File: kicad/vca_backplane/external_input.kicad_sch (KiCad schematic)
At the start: 6 parts, among them J10 AudioJack_729JH, U13 TL072

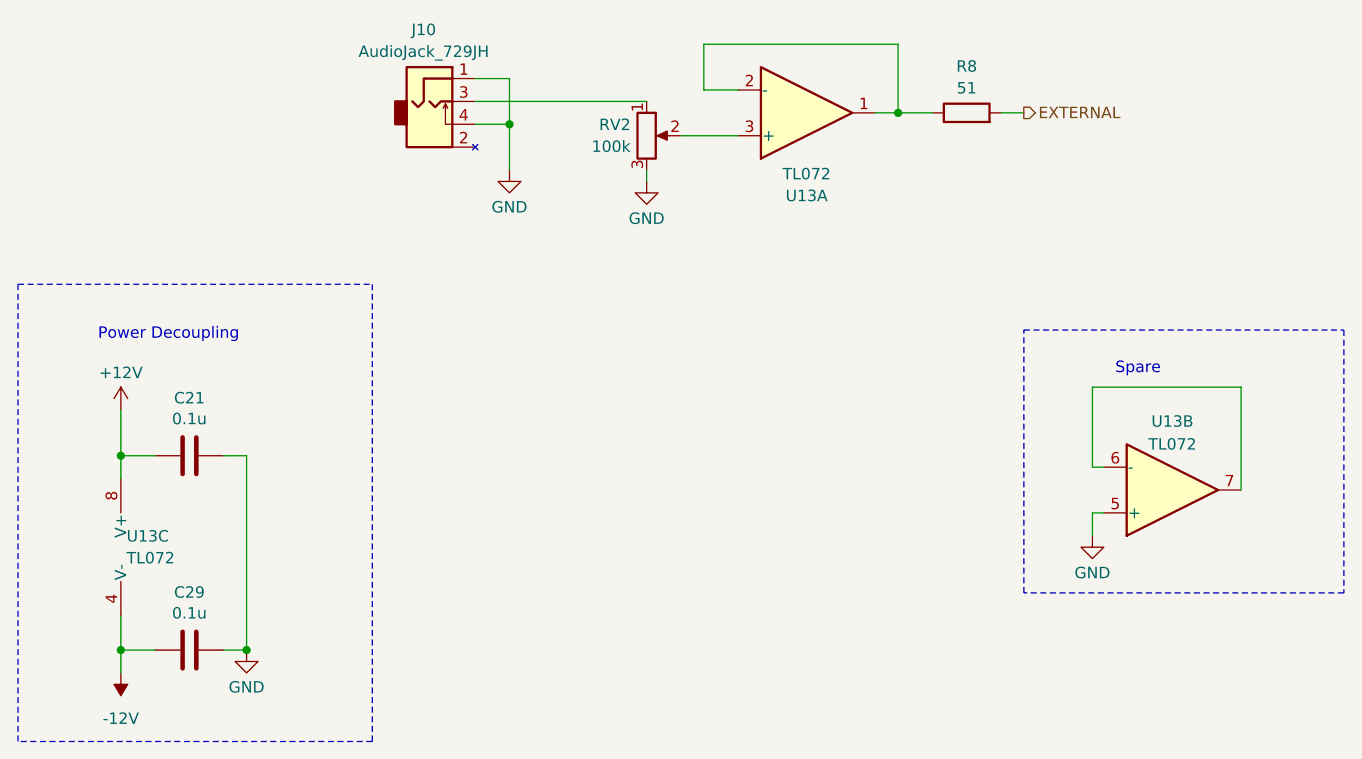
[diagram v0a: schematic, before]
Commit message: geographically reorientated from pcb
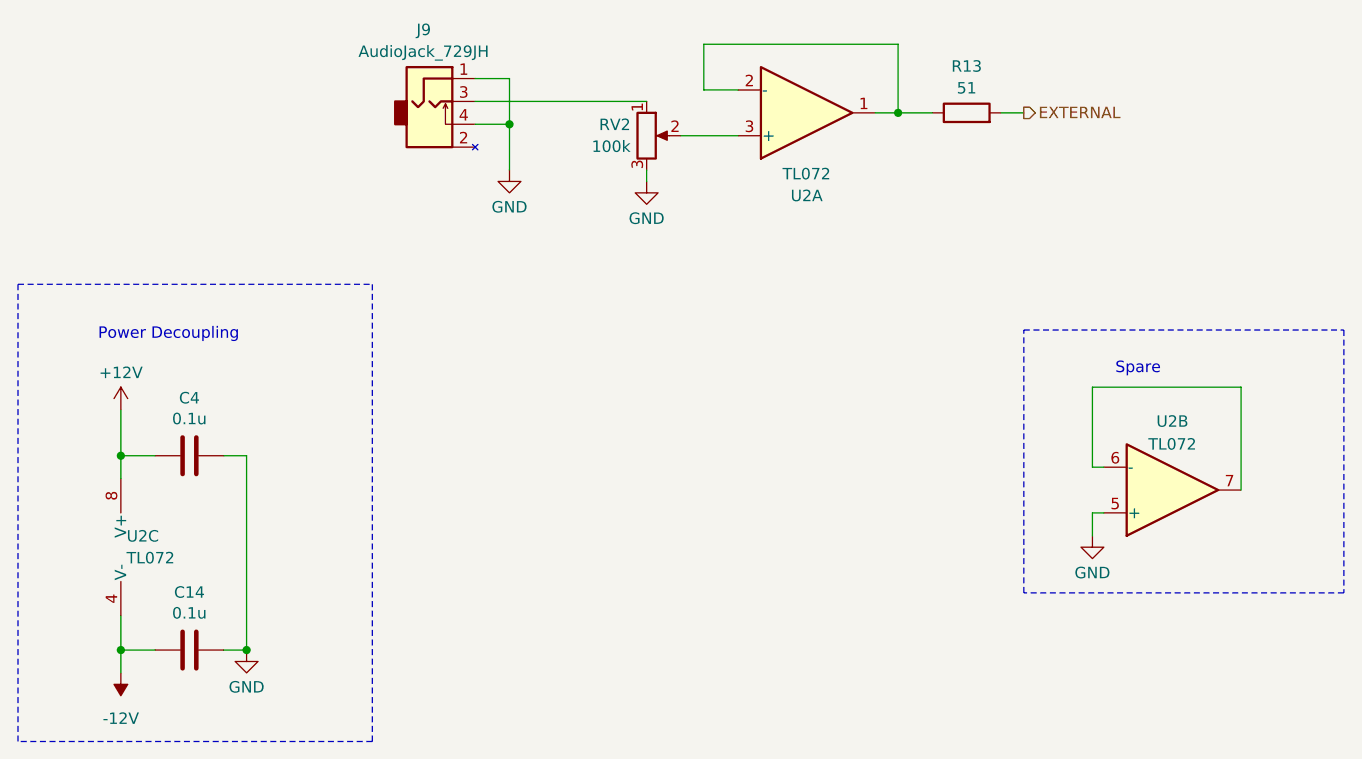
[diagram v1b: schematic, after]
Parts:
- renumbered C29 to C14, C21 to C4, J10 to J9, R8 to R13, U13 to U2
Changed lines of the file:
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@@
   (symbol (lib_id "vca_backplane:AudioJack_729JH") (at 93.98 119.38 0) (unit 1)
     (in_bom yes) (on_board yes) (dnp no) (fields_autoplaced)
-    (property "Reference" "J10" (at 93.345 111.4257 0)
+    (property "Reference" "J9" (at 93.345 111.4257 0)
       (effects (font (size 1.27 1.27)))
     )
@@
       (project "vca_backplane"
         (path "/bdbd6910-8f28-459f-89ba-e6dd447d59a9/5428edbd-a37e-4081-9b79-56dfae2e2a66"
-          (reference "J10") (unit 1)
+          (reference "J9") (unit 1)
         )
       )
@@
   (symbol (lib_id "Device:C") (at 67.31 158.75 270) (unit 1)
     (in_bom yes) (on_board yes) (dnp no)
-    (property "Reference" "C21" (at 67.31 152.3492 90)
+    (property "Reference" "C4" (at 67.31 152.3492 90)
       (effects (font (size 1.27 1.27)))
     )
@@
       (project "vca_backplane"
         (path "/bdbd6910-8f28-459f-89ba-e6dd447d59a9/5428edbd-a37e-4081-9b79-56dfae2e2a66"
-          (reference "C21") (unit 1)
+          (reference "C4") (unit 1)
         )
       )
@@
   (symbol (lib_id "Device:R") (at 153.67 120.65 90) (unit 1)
     (in_bom yes) (on_board yes) (dnp no) (fields_autoplaced)
-    (property "Reference" "R8" (at 153.67 115.4897 90)
+    (property "Reference" "R13" (at 153.67 115.4897 90)
       (effects (font (size 1.27 1.27)))
     )
@@
       (project "vca_backplane"
         (path "/bdbd6910-8f28-459f-89ba-e6dd447d59a9/5428edbd-a37e-4081-9b79-56dfae2e2a66"
-          (reference "R8") (unit 1)
+          (reference "R13") (unit 1)
         )
       )
@@
   (symbol (lib_id "Amplifier_Operational:TL072") (at 135.89 120.65 0) (mirror x) (unit 1)
     (in_bom yes) (on_board yes) (dnp no)
-    (property "Reference" "U13" (at 135.89 129.8743 0)
+    (property "Reference" "U2" (at 135.89 129.8743 0)
       (effects (font (size 1.27 1.27)))
     )
@@
       (project "vca_backplane"
         (path "/bdbd6910-8f28-459f-89ba-e6dd447d59a9/5428edbd-a37e-4081-9b79-56dfae2e2a66"
-          (reference "U13") (unit 1)
+          (reference "U2") (unit 1)
         )
       )
@@
   (symbol (lib_id "Device:C") (at 67.31 180.34 270) (unit 1)
     (in_bom yes) (on_board yes) (dnp no)
-    (property "Reference" "C29" (at 67.31 173.9392 90)
+    (property "Reference" "C14" (at 67.31 173.9392 90)
       (effects (font (size 1.27 1.27)))
     )
@@
       (project "vca_backplane"
         (path "/bdbd6910-8f28-459f-89ba-e6dd447d59a9/5428edbd-a37e-4081-9b79-56dfae2e2a66"
-          (reference "C29") (unit 1)
+          (reference "C14") (unit 1)
         )
       )
@@
   (symbol (lib_id "Amplifier_Operational:TL072") (at 62.23 168.91 0) (unit 3)
     (in_bom yes) (on_board yes) (dnp no) (fields_autoplaced)
-    (property "Reference" "U13" (at 60.325 167.6979 0)
+    (property "Reference" "U2" (at 60.325 167.6979 0)
       (effects (font (size 1.27 1.27)) (justify left))
     )
@@
       (project "vca_backplane"
         (path "/bdbd6910-8f28-459f-89ba-e6dd447d59a9/5428edbd-a37e-4081-9b79-56dfae2e2a66"
-          (reference "U13") (unit 3)
+          (reference "U2") (unit 3)
         )
       )
@@
   (symbol (lib_id "Amplifier_Operational:TL072") (at 176.53 162.56 0) (mirror x) (unit 2)
     (in_bom yes) (on_board yes) (dnp no)
-    (property "Reference" "U13" (at 176.53 154.94 0)
+    (property "Reference" "U2" (at 176.53 154.94 0)
       (effects (font (size 1.27 1.27)))
     )
@@
       (project "vca_backplane"
         (path "/bdbd6910-8f28-459f-89ba-e6dd447d59a9/5428edbd-a37e-4081-9b79-56dfae2e2a66"
-          (reference "U13") (unit 2)
-        )
-      )
+          (reference "U2") (unit 2)
+        )
+      )

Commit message: checkin before moving pi footprint a bit
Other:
- company: (none) -> Zoxnoxious Engineering
- title: (none) -> Zoxnoxious Backplane and VCA
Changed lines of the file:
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@@
 (kicad_sch (version 20230121) (generator eeschema)
   (paper "B")
+  (title_block
+    (title "Zoxnoxious Backplane and VCA")
+    (date "2025-06-03")
+    (rev "0.3")
+    (company "Zoxnoxious Engineering")
+  )
   (junction (at 102.87 121.92) (diameter 0) (color 0 0 0 0)
   )
